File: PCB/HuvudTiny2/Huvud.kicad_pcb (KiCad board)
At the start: 4 copper layers, 42 x 42 mm, 101 parts, among them J1 MOLEX Micro Fit 2x3, J2 DBG, J3 THERM, J4 FAN0, J5 FAN1, J6 Heater, J7 Endstop, J8 THERM, J9 STEPPER, Q1 AO3400A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

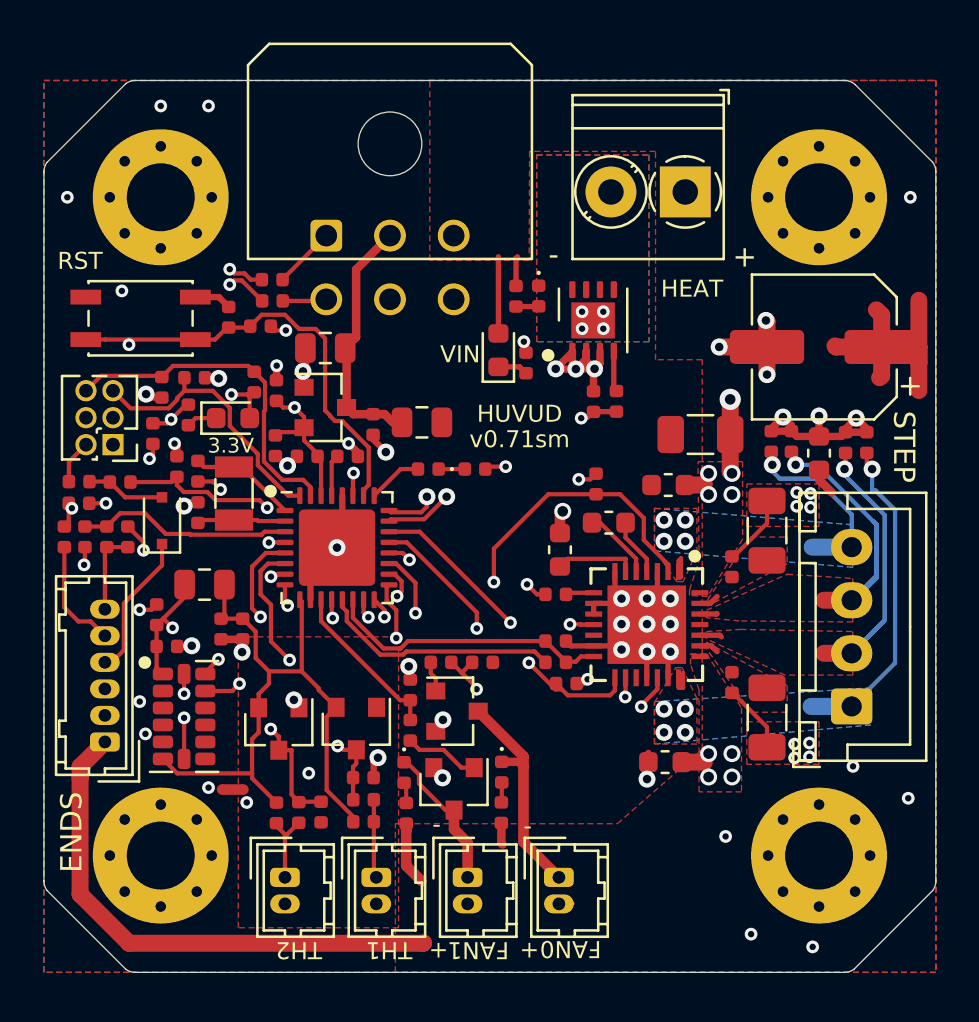
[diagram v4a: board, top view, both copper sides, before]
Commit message: Updated GNDA layout.
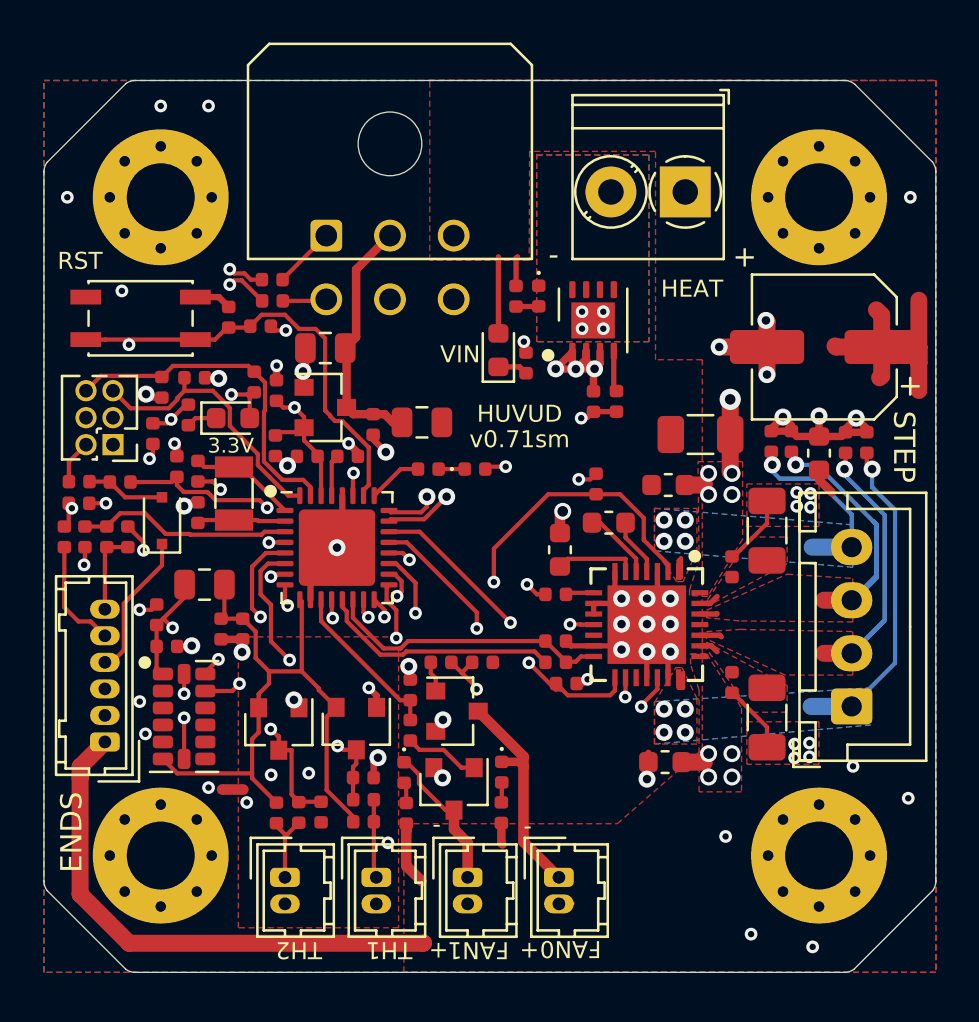
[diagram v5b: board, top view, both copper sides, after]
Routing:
- net HEATER: track 30.4 -> 26.7 mm
- net GNDA: track 3.13 -> 4.20 mm, vias 5 -> 8
- net FAN0: track 14.0 -> 14.7 mm
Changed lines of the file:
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@@
   (segment (start 191.36 126.315) (end 191.36 126.89) (width 0.35) (layer "F.Cu") (net 1))
   (segment (start 191.36 126.89) (end 191.33 126.92) (width 0.35) (layer "F.Cu") (net 1))
+  (segment (start 197.66 129.52) (end 197.66 128.96) (width 0.3) (layer "F.Cu") (net 1))
   (segment (start 197.525 132.83) (end 197.525 132.095) (width 0.3) (layer "F.Cu") (net 1))
   (segment (start 190.34 126.315) (end 191.36 126.315) (width 0.35) (layer "F.Cu") (net 1))
   (segment (start 194.01 129.41) (end 193.77 129.17) (width 0.3) (layer "F.Cu") (net 1))
+  (segment (start 197.66 128.96) (end 197.3 128.6) (width 0.3) (layer "F.Cu") (net 1))
   (via (at 197.73 131.89) (size 0.8) (drill 0.4) (layers "F.Cu" "B.Cu") (net 1))
   (via (at 191.33 126.92) (size 0.8) (drill 0.4) (layers "F.Cu" "B.Cu") (net 1))
   (via (at 194.47 132.62) (size 0.6) (drill 0.3) (layers "F.Cu" "B.Cu") (free) (net 1))
   (via (at 191.55 134) (size 0.6) (drill 0.3) (layers "F.Cu" "B.Cu") (free) (net 1))
+  (via (at 197.3 128.6) (size 0.6) (drill 0.3) (layers "F.Cu" "B.Cu") (net 1))
   (via (at 193.77 129.17) (size 0.8) (drill 0.4) (layers "F.Cu" "B.Cu") (net 1))
+  (via (at 192.7 132.7) (size 0.6) (drill 0.3) (layers "F.Cu" "B.Cu") (free) (net 1))
+  (via (at 198.2 135.9) (size 0.6) (drill 0.3) (layers "F.Cu" "B.Cu") (free) (net 1))
   (segment (start 214.485 122.415) (end 216.05 120.85) (width 0.2) (layer "F.Cu") (net 2))
   (segment (start 188.8 115.265) (end 188.685 115.265) (width 0.2) (layer "F.Cu") (net 2))
@@
   (via (at 207.3 115.9) (size 0.6) (drill 0.3) (layers "F.Cu" "B.Cu") (net 19))
   (via (at 192.6895 123.368276) (size 0.6) (drill 0.3) (layers "F.Cu" "B.Cu") (net 19))
-  (segment (start 198.9 116.6) (end 199.1 116.8) (width 0.2) (layer "In1.Cu") (net 19))
-  (segment (start 199.1 119.9) (end 200.5 121.3) (width 0.2) (layer "In1.Cu") (net 19))
   (segment (start 192.6895 123.368276) (end 192.6895 123.1895) (width 0.2) (layer "In1.Cu") (net 19))
-  (segment (start 191.4 118.8) (end 193.2 117) (width 0.2) (layer "In1.Cu") (net 19))
-  (segment (start 191.4 121.9) (end 191.4 118.8) (width 0.2) (layer "In1.Cu") (net 19))
-  (segment (start 201.9 121.3) (end 207.3 115.9) (width 0.2) (layer "In1.Cu") (net 19))
-  (segment (start 192.6895 123.1895) (end 191.4 121.9) (width 0.2) (layer "In1.Cu") (net 19))
-  (segment (start 200.5 121.3) (end 201.3 121.3) (width 0.2) (layer "In1.Cu") (net 19))
-  (segment (start 193.2 117) (end 193.6 116.6) (width 0.2) (layer "In1.Cu") (net 19))
-  (segment (start 201.3 121.3) (end 201.9 121.3) (width 0.2) (layer "In1.Cu") (net 19))
-  (segment (start 199.1 116.8) (end 199.1 119.9) (width 0.2) (layer "In1.Cu") (net 19))
-  (segment (start 193.6 116.6) (end 198.9 116.6) (width 0.2) (layer "In1.Cu") (net 19))
+  (segment (start 202.65 120.55) (end 207.3 115.9) (width 0.2) (layer "In1.Cu") (net 19))
+  (segment (start 194.8 119.3) (end 196.2 117.9) (width 0.2) (layer "In1.Cu") (net 19))
+  (segment (start 191.2 121.7) (end 191.2 119.7) (width 0.2) (layer "In1.Cu") (net 19))
+  (segment (start 197.1 117.9) (end 199.75 120.55) (width 0.2) (layer "In1.Cu") (net 19))
+  (segment (start 191.6 119.3) (end 194.8 119.3) (width 0.2) (layer "In1.Cu") (net 19))
+  (segment (start 199.75 120.55) (end 202.65 120.55) (width 0.2) (layer "In1.Cu") (net 19))
+  (segment (start 191.2 119.7) (end 191.6 119.3) (width 0.2) (layer "In1.Cu") (net 19))
+  (segment (start 192.6895 123.1895) (end 191.2 121.7) (width 0.2) (layer "In1.Cu") (net 19))
+  (segment (start 196.2 117.9) (end 197.1 117.9) (width 0.2) (layer "In1.Cu") (net 19))
   (segment (start 202.3828 125.8056) (end 202.3828 125.0469) (width 0.2) (layer "F.Cu") (net 20))
   (segment (start 199.0859 121.75) (end 198.25 121.75) (width 0.2) (layer "F.Cu") (net 20))
@@
   (via (at 202.3737 128.6665) (size 0.6) (drill 0.3) (layers "F.Cu" "B.Cu") (net 38))
   (via (at 193.4776 124.7268) (size 0.6) (drill 0.3) (layers "F.Cu" "B.Cu") (net 38))
-  (segment (start 193.4776 124.7268) (end 197.4173 128.6665) (width 0.2) (layer "In1.Cu") (net 38))
-  (segment (start 197.4173 128.6665) (end 202.3737 128.6665) (width 0.2) (layer "In1.Cu") (net 38))
+  (segment (start 198.3 128.1) (end 198.8665 128.6665) (width 0.2) (layer "In1.Cu") (net 38))
+  (segment (start 195.4254 126.6746) (end 197.9746 126.6746) (width 0.2) (layer "In1.Cu") (net 38))
+  (segment (start 198.8665 128.6665) (end 202.3737 128.6665) (width 0.2) (layer "In1.Cu") (net 38))
+  (segment (start 193.4776 124.7268) (end 195.4254 126.6746) (width 0.2) (layer "In1.Cu") (net 38))
+  (segment (start 198.3 127) (end 198.3 128.1) (width 0.2) (layer "In1.Cu") (net 38))
+  (segment (start 197.9746 126.6746) (end 198.3 127) (width 0.2) (layer "In1.Cu") (net 38))
   (segment (start 198.7753 129.185) (end 199.25 129.185) (width 0.2) (layer "F.Cu") (net 39))
   (segment (start 195.05 124.45) (end 195.05 125.4597) (width 0.2) (layer "F.Cu") (net 39))
@@
   (via (at 212.2 130.7) (size 0.8) (drill 0.4) (layers "F.Cu" "B.Cu") (net 40))
   (via (at 221 118.3) (size 0.8) (drill 0.4) (layers "F.Cu" "B.Cu") (net 40))
+  (segment (start 221 119.15) (end 222.08 120.23) (width 0.2) (layer "B.Cu") (net 40))
+  (segment (start 222.08 127.4345) (end 220.0385 129.476) (width 0.2) (layer "B.Cu") (net 40))
   (segment (start 222.08 120.23) (end 222.08 127.4345) (width 0.2) (layer "B.Cu") (net 40))
   (segment (start 220.038 129.476) (end 218.124 129.476) (width 0.8) (layer "B.Cu") (net 40))
-  (segment (start 222.08 127.4345) (end 220.0385 129.476) (width 0.2) (layer "B.Cu") (net 40))
-  (segment (start 221 118.3) (end 221 119.31) (width 0.2) (layer "B.Cu") (net 40))
-  (segment (start 221 119.31) (end 221.16 119.31) (width 0.2) (layer "B.Cu") (net 40))
-  (segment (start 221.16 119.31) (end 222.08 120.23) (width 0.2) (layer "B.Cu") (net 40))
+  (segment (start 221 118.3) (end 221 119.15) (width 0.2) (layer "B.Cu") (net 40))
   (segment (start 212.888 126.125) (end 212.8878 126.1248) (width 0.2) (layer "F.Cu") (net 41))
   (segment (start 219.75 117.535) (end 219.75 118.25) (width 0.2) (layer "F.Cu") (net 41))
@@
       (pts
         (xy 224 142)
-        (xy 198.55 142)
-        (xy 198.55 135)
+        (xy 198.95 142)
+        (xy 198.95 135)
         (xy 209 135)
         (xy 213 131.5)
@@
   (zone (net 1) (net_name "GNDA") (layer "F.Cu") (hatch edge 0.508)
     (priority 3)
-    (connect_pads (clearance 0.378))
+    (connect_pads (clearance 0.254))
     (min_thickness 0.254) (filled_areas_thickness no)
     (fill yes (thermal_gap 0.508) (thermal_bridge_width 0.378))
@@
     (polygon
       (pts
-        (xy 205.5 110.22)
+        (xy 199 110.22)
         (xy 186 110.22)
         (xy 186 142)
         (xy 182 142)
         (xy 182 100)
-        (xy 205.5 100)
+        (xy 199 100)
       )
     )
@@
         (xy 206 134.35)
         (xy 206 132.5)
-        (xy 206 111.5)
-        (xy 206 100)
+        (xy 206 109.5)
+        (xy 199.7 109.5)
+        (xy 199.7 100)
         (xy 224 100)
       )

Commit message: Update screw terminal to molex connector.
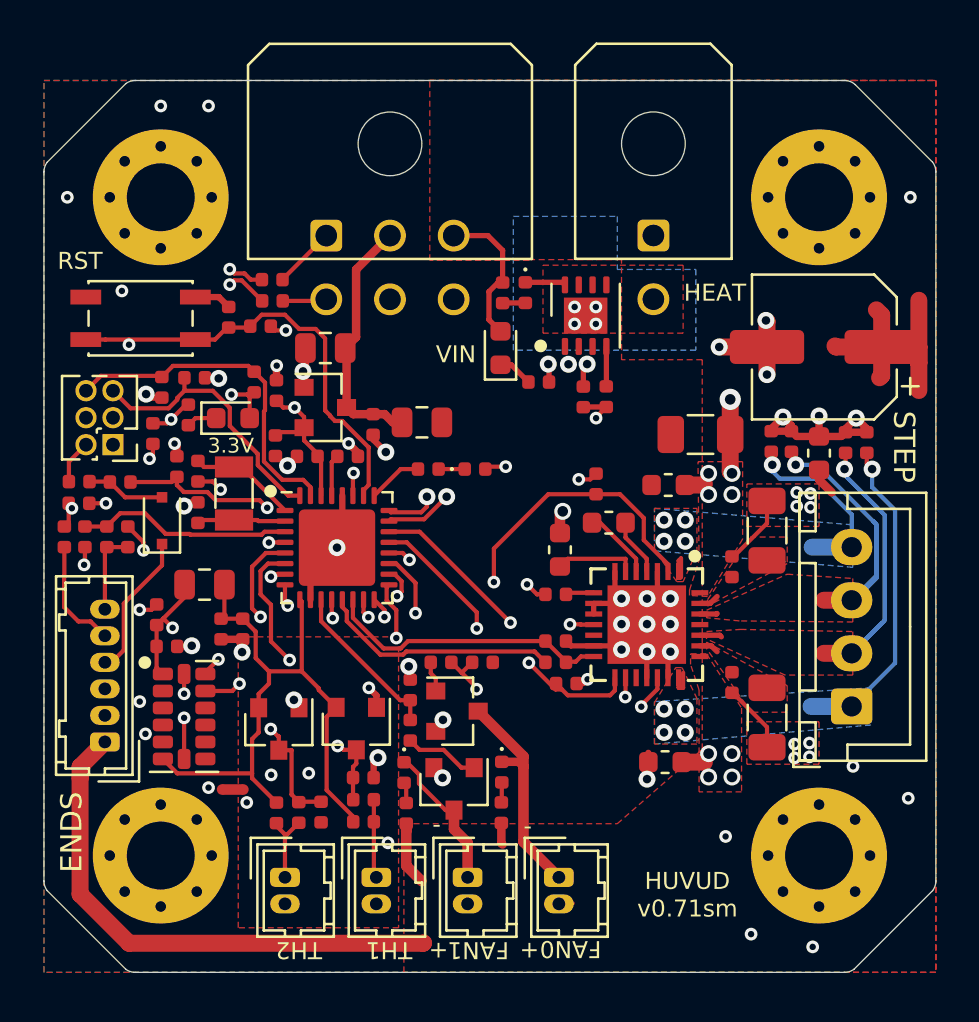
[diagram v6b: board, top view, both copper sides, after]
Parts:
- J6: footprint Huvud:TerminalBlock_Phoenix_PT-1,5-2-3.5-H_1x02_P3.50mm_Horizontal -> Connector_Molex:Molex_Micro-Fit_3.0_43045-0200_2x01_P3.00mm_Horizontal
- moved J6 2.54 mm to (210.7, 107.3), turned to 0 degrees
- moved R11 1.08 mm to (205.3, 114.2), turned to 0 degrees
- moved D3 0.65 mm to (204.7, 110.0)
- moved R15 0.65 mm to (203.6, 110.0)
- moved R28 0.53 mm to (208.5, 114.9)
- moved R12 0.53 mm to (207.4, 114.9)
- moved Q3 0.42 mm to (207.5, 111.1)
- moved D6 0.14 mm to (203.5, 112.6)
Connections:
- J2 pad 1: (no net) -> unconnected-(J2-Pad1)
- U1 pad 10: (no net) -> unconnected-(U1-Pad10)
- U1 pad 11: (no net) -> unconnected-(U1-Pad11)
- U1 pad 3: (no net) -> unconnected-(U1-Pad3)
- U1 pad 8: (no net) -> unconnected-(U1-Pad8)
- U1 pad 9: (no net) -> unconnected-(U1-Pad9)
- U2 pad 12: (no net) -> unconnected-(U2-Pad12)
- U2 pad 17: (no net) -> unconnected-(U2-Pad17)
- U2 pad 25: (no net) -> unconnected-(U2-Pad25)
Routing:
- net GND: track 66.0 -> 58.8 mm, vias 55 -> 54
- net ST_VS: track 60.3 -> 62.3 mm
- net Net-(D3-Pad1): track 0.00 -> 1.91 mm
- net HEATER: track 26.7 -> 27.4 mm

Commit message: Finished routing.
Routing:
- net /ST_B1: track 16.2 -> 12.6 mm
- net /ST_A1: track 15.3 -> 13.7 mm
- net ENDSTOP2: track 19.8 -> 20.8 mm
- net Net-(C3-Pad1): track 4.14 -> 4.75 mm
- net VCC_IO: track 19.5 -> 20.1 mm
- net USBD+: track 20.4 -> 19.9 mm

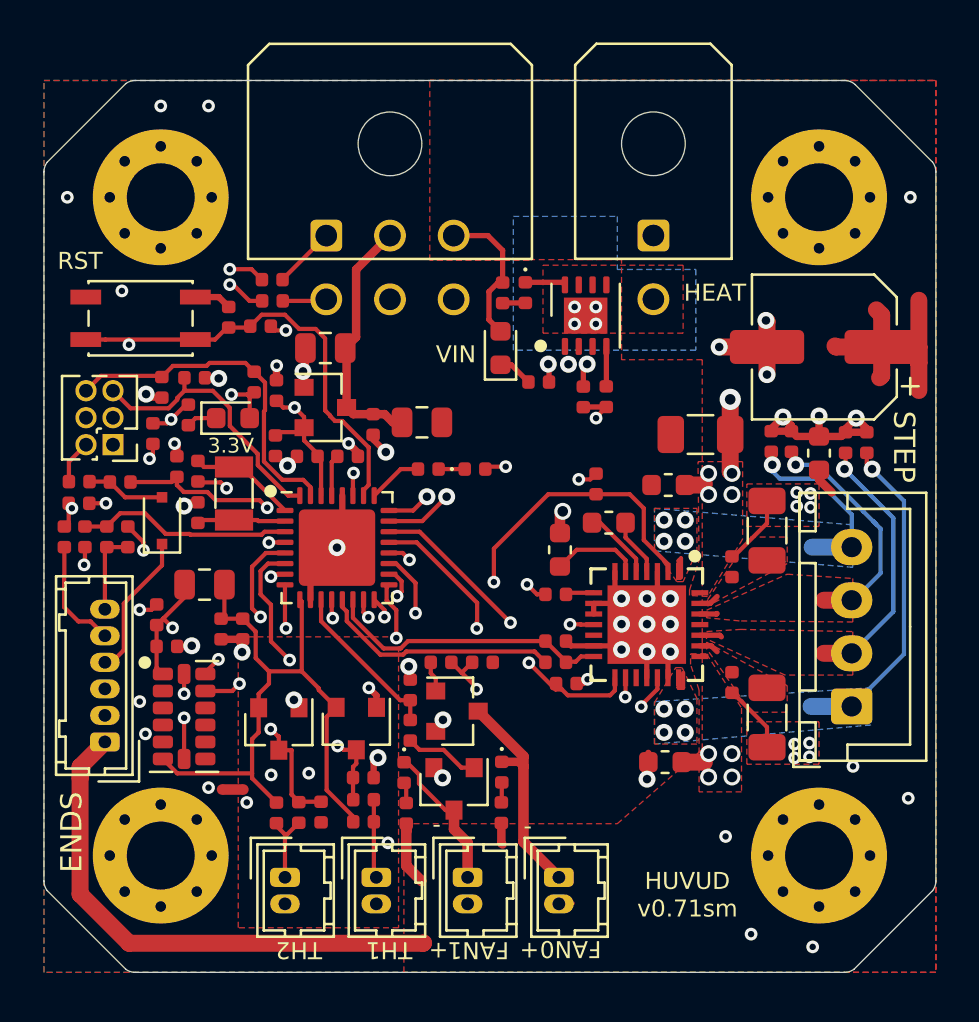
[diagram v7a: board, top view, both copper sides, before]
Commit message: Clean PCB routing.
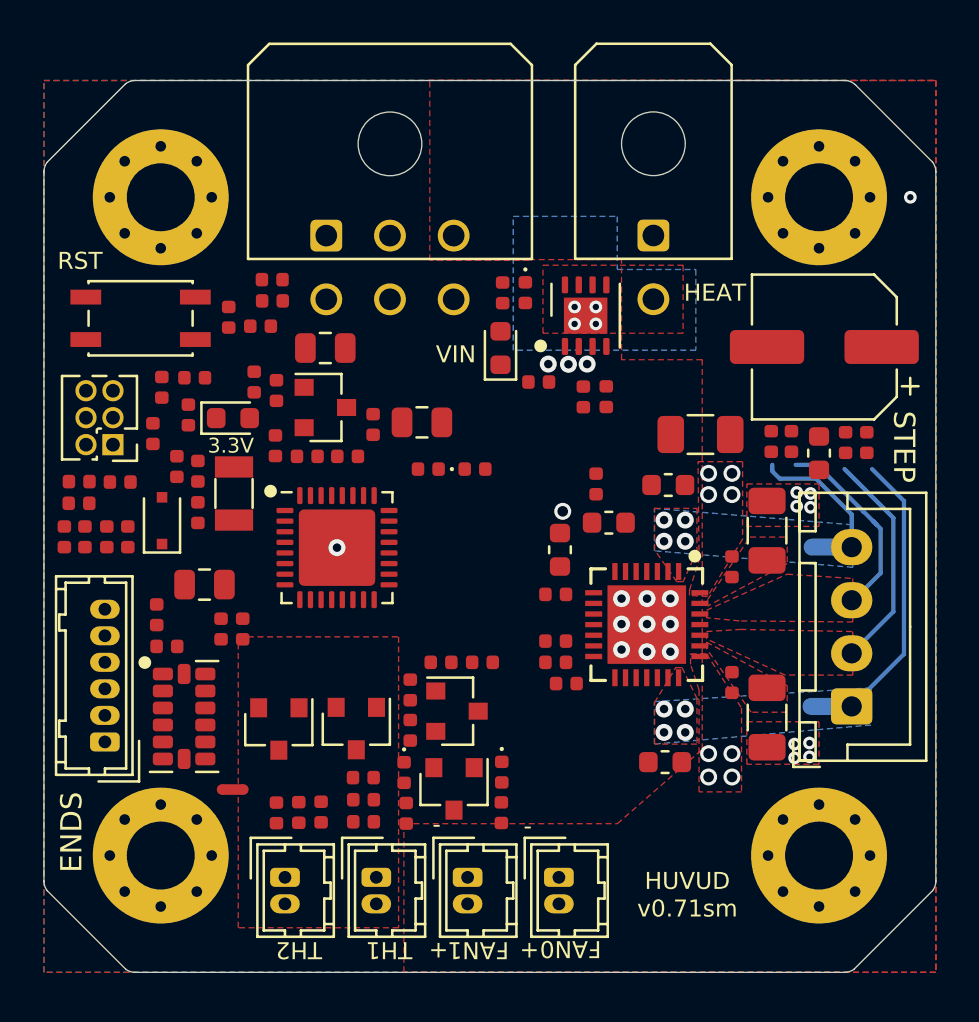
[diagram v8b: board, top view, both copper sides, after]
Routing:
- net ST_VS: track 62.3 -> 0.00 mm, vias 16 -> 10
- net GND: track 59.1 -> 0.00 mm, vias 54 -> 21
- net AREF: track 30.5 -> 0.00 mm
- net +3V3: track 29.1 -> 0.00 mm, vias 8 -> 0
- net ST_EN: track 22.6 -> 0.00 mm, vias 2 -> 0
- net NRST: track 24.8 -> 3.83 mm, vias 1 -> 0
- net ST_DIAG: track 18.8 -> 0.00 mm, vias 2 -> 0
- net ACS: track 17.9 -> 0.00 mm, vias 2 -> 0
- net ST_DIR: track 17.6 -> 0.00 mm, vias 2 -> 0
- net SWCLK: track 16.2 -> 0.00 mm
- net ST_STEP: track 15.8 -> 0.00 mm, vias 2 -> 0
- net SCL: track 14.8 -> 0.00 mm, vias 2 -> 0
- net SDO: track 13.9 -> 0.00 mm, vias 2 -> 0
- net ST_UART_RX: track 13.5 -> 0.00 mm
- net SWDIO: track 13.0 -> 0.00 mm
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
